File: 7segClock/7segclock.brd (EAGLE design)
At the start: 100 x 100 mm, 19 parts, among them J1 ICSP, J2 ZX62R-AB-5P, Q1 CSTNE16M0V530000R0, U1 ATMEGA328P-AU-TQFP32, U2 TM1640, U3 CP2104

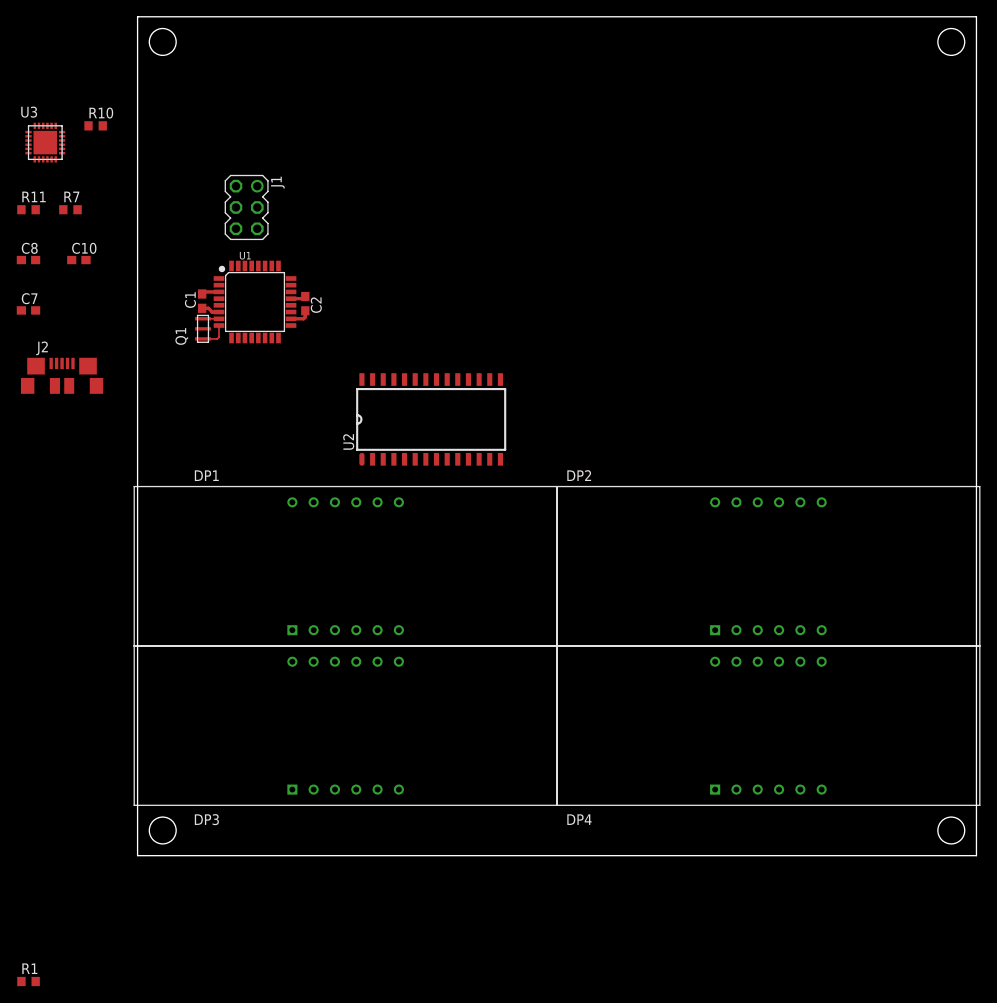
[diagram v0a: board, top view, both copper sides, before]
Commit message: [add]add 7seg clokc before autoroute
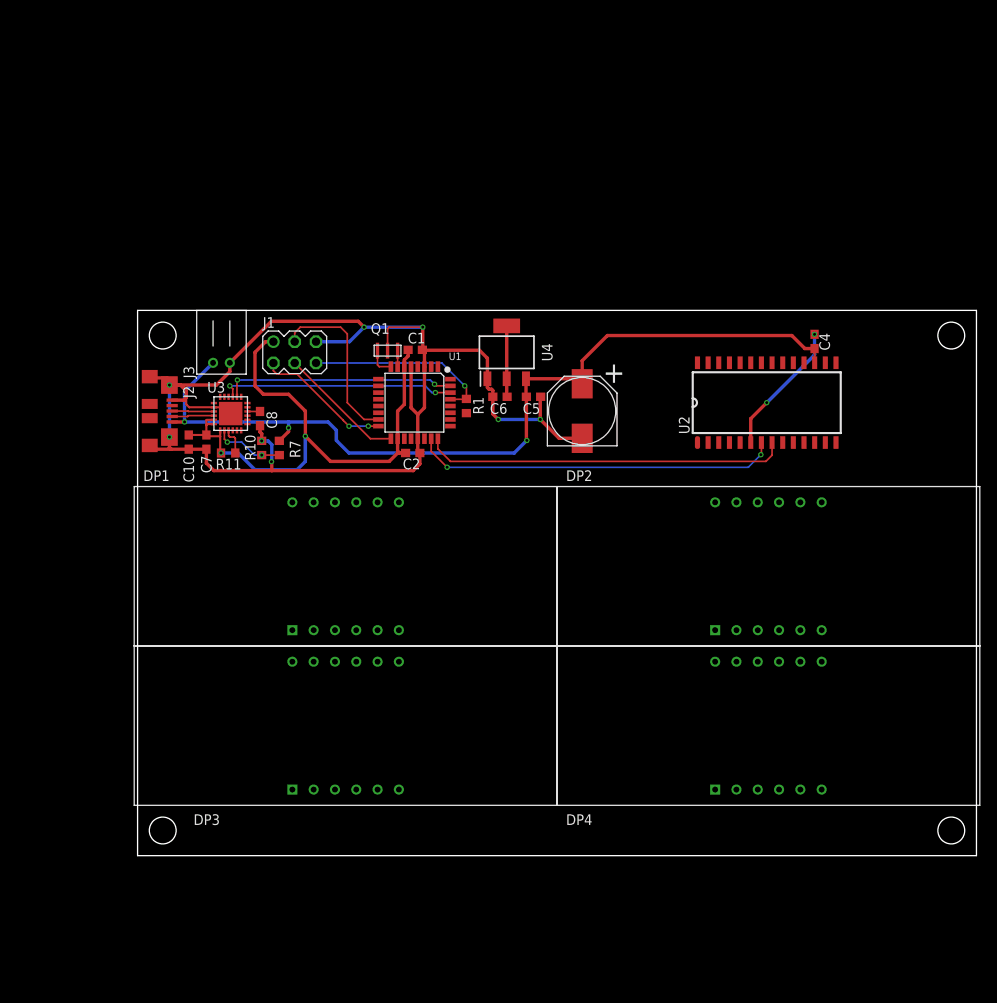
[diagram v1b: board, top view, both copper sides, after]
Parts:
- added C3: UWT1E221MNL1GS, taki-library:NICHICON-ALMINUM-CAPACITOR-8MM
- added C4: (no value), taki-library:C0603
- added C5, C6: 10uF, taki-library:C0603
- added J3: S2B-PH-K-S, taki-library:S2B-PH-K-S
- added U4: ADP3338AKCZ-3.3, taki-library:SOT233
- moved R1 86.2 mm to (39.2, 53.6), turned to 270 degrees
- moved R10 43.2 mm to (14.8, 48.6), turned to 270 degrees
- moved U2 40.0 mm to (75.0, 54.0)
- moved U3 39.1 mm to (11.1, 52.7)
- moved R7 37.8 mm to (16.9, 48.6), turned to 90 degrees
- moved R11 37.5 mm to (10.8, 48.0), turned to 180 degrees
- moved C8 33.5 mm to (14.6, 52.1), turned to 270 degrees
- moved C7 26.4 mm to (8.20, 49.3), turned to 270 degrees
- moved C1 26.1 mm to (33.1, 60.3), turned to 0 degrees
- moved C10 25.3 mm to (6.10, 49.3), turned to 270 degrees
- moved U1 22.5 mm to (33.0, 54.0), turned to 270 degrees
- moved Q1 22.2 mm to (29.8, 60.2), turned to 0 degrees
- moved C2 21.9 mm to (32.8, 48.0), turned to 0 degrees
- moved J1 17.5 mm to (20.0, 60.0), turned to 0 degrees
- moved J2 10.9 mm to (1.45, 53.0), turned to 270 degrees
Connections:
- removed net ESP32_RX: U3.21
- removed net ESP32_TX: U3.20
- removed net VBUS: J2.VCC, R7.2
- new net +5V: C3.POS, C4.1, C5.1, J2.VCC, J3.1, R7.2, U2.17, U4.3
- new net ATMEGA_RX: U1.30, U3.21
- new net ATMEGA_TX: U1.31, U3.20
- new net DIN: U1.23, U2.7
- new net SCLK: U1.24, U2.8
- net +3V3: now also C6.1, U4.2, U4.4
- net GND: now also C3.NEG, C4.2, C5.2, C6.2, J3.2, U2.6, U4.1
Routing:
- net GND: track 3.92 -> 179.5 mm, vias 0 -> 10
- net +5V: track 0.00 -> 104.7 mm, vias 0 -> 3
- net +3V3: track 4.73 -> 76.6 mm, vias 0 -> 2
- net DIN: track 0.00 -> 43.7 mm, vias 0 -> 2
- net SCLK: track 0.00 -> 43.5 mm
- net ATMEGA_RX: track 0.00 -> 28.1 mm, vias 0 -> 2
- net ATMEGA_TX: track 0.00 -> 27.7 mm, vias 0 -> 2
- net RST: track 0.00 -> 22.4 mm, vias 0 -> 1
- net MOSI: track 0.00 -> 20.7 mm
- net MISO: track 0.00 -> 16.2 mm, vias 0 -> 2
- net SCK: track 0.00 -> 15.2 mm
- net N$12: track 0.00 -> 8.39 mm, vias 0 -> 2
- net D_N: track 0.00 -> 5.02 mm
- net D_P: track 0.00 -> 5.00 mm
- net N$13: track 0.00 -> 3.32 mm
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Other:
- board size 100 x 100 mm -> 100 x 65 mm

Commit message: [add]add gerver output of 7seg clokc
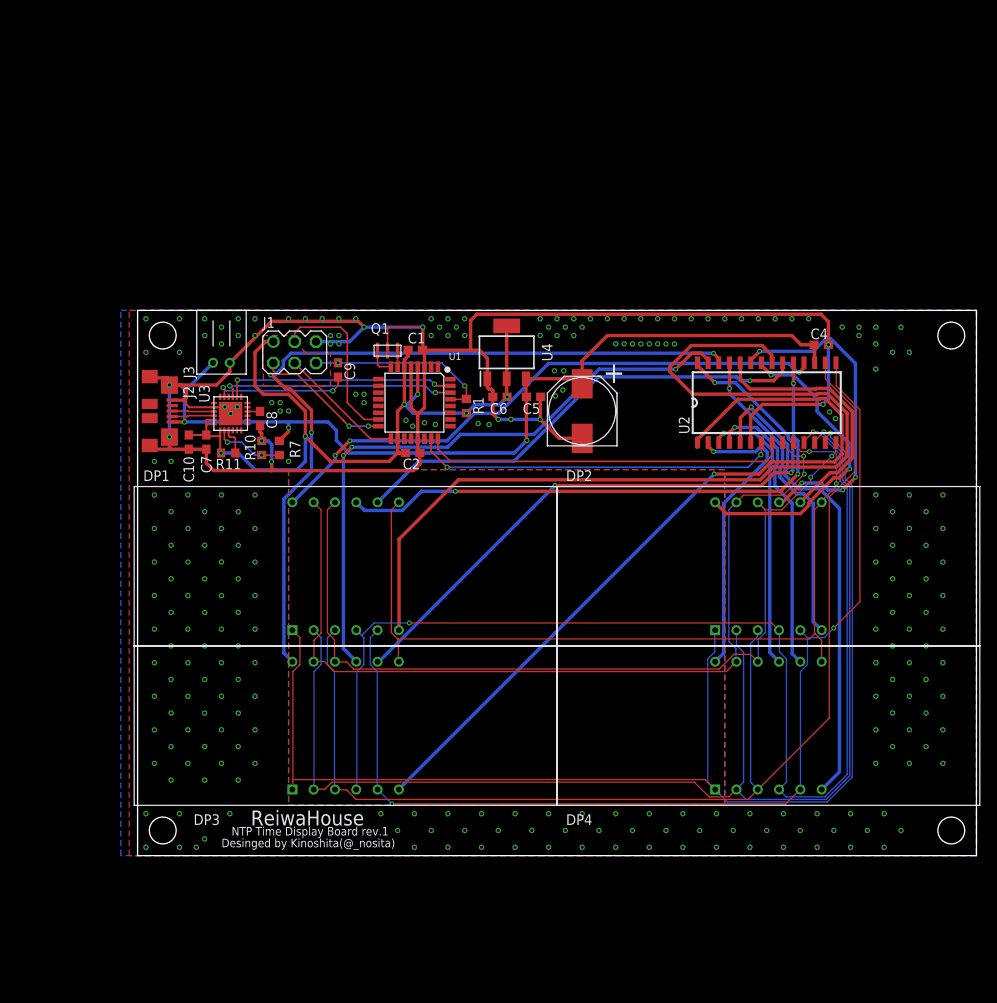
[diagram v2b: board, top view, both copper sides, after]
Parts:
- added C9: 0.1uF, taki-library:C0603
- C1, C2: value (none) -> 0.1uF
- moved C4 0.89 mm to (81.5, 60.9), turned to 0 degrees
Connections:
- removed net CTS: U3.18
- new net DTR: C9.2, U3.23
- net RST: now also C9.1
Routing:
- net N$5: track 0.00 -> 151.9 mm, vias 0 -> 1
- net N$4: track 0.00 -> 150.4 mm, vias 0 -> 1
- net N$8: track 0.00 -> 148.1 mm
- net N$3: track 0.00 -> 144.3 mm, vias 0 -> 2
- net N$7: track 0.00 -> 128.9 mm, vias 0 -> 2
- net GRID4: track 0.00 -> 111.9 mm
- net N$1: track 0.00 -> 105.8 mm, vias 0 -> 2
- net N$6: track 0.00 -> 105.3 mm, vias 0 -> 2
- net N$2: track 0.00 -> 101.7 mm, vias 0 -> 2
- net GRID12: track 0.00 -> 94.5 mm, vias 0 -> 1
- net GRID9: track 0.00 -> 94.0 mm, vias 0 -> 3
- net GRID11: track 0.00 -> 77.9 mm, vias 0 -> 3
- net GRID10: track 0.00 -> 74.4 mm, vias 0 -> 3
- net GRID1: track 0.00 -> 69.4 mm, vias 0 -> 3
- net GRID2: track 0.00 -> 68.3 mm, vias 0 -> 3
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- added copper zone on layer 1, net GND
- added copper zone on layer 16, net GND
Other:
- board text added: "Desinged by Kinoshita(@_nosita)"
- board text added: "NTP Time Display Board rev.1"
- board text added: "ReiwaHouse"
